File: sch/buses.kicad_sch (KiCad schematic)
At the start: 20 parts, among them U1 74AC00, U2 74HC74, U3 DS1135Z, U4 74LS32, U5 74LS11

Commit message: New address decoder
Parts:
- added unit 1 of U1
- C10, C9: value 100nF -> (none)
- C5, C6, C7, C8: value 10nF -> (none)
- D1: value 1N5817 -> (none)
- R1: value ~ -> (none)
- U1: value 74AC00 -> (none); footprint Package_SO:TSSOP-14_4.4x5mm_P0.65mm -> (none)
- U2: value 74HC74 -> (none)
- U3: value DS1135Z -> (none)
- U3: value DS1135Z -> (none); footprint Package_SO:SO-8_5.3x6.2mm_P1.27mm -> (none)
- U4: value 74LS32 -> (none)
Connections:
- net +5V: no longer U4.4, U4.5
- net CLK: now also U4.4
- net CPU_R/~{W}: now also U4.5, U1.1, U1.2; no longer BDT1.1 (A->B)
- net MEM_WR: now reaches U4.6
- net BUS_IN_EN renamed DATA_BUS_EN
- net CPU_BUS_ENABLE renamed CPU_BUS_EN
- net LATCH_~{Load}: no longer names the net of LATCH1.11 (Load), U5.6
- net LATCH_~{OE}: no longer names the net of LATCH1.1 (OE), U1.8, U4.2
- new net CPU_W/~{R}: BDT1.1 (A->B), U1.3
- no-connect marks 9 -> 8
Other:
- moved on the sheet: D1, R1, U1B, U1C, U1D, U2A, U3A, U4A, U4B, U5A, U5B

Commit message: Board layout, addr bus
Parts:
- removed RP3, RP4, RP5: 1K, Resistor_THT:R_Array_SIP9, symbol Device:R_Network08
- added R12, R13, R14, R15, R16, R17, R18, R19, R20, R21, R22, R23, R32, R33, R34, R35: 1K, Resistor_SMD:R_0603_1608Metric, symbol Device:R
- added R3: 10K, Resistor_SMD:R_1206_3216Metric_Pad1.30x1.75mm_HandSolder, symbol Device:R
- C10, C9: value (none) -> 100nF; footprint (none) -> Capacitor_SMD:C_1206_3216Metric_Pad1.33x1.80mm_HandSolder
- C5, C6, C7, C8: value (none) -> 10nF; footprint (none) -> Capacitor_SMD:C_1206_3216Metric_Pad1.33x1.80mm_HandSolder
- D1: value (none) -> 1N5817; footprint (none) -> Diode_THT:D_A-405_P7.62mm_Horizontal
- R1: value (none) -> 1K; footprint (none) -> Resistor_SMD:R_1206_3216Metric_Pad1.30x1.75mm_HandSolder
- RP1, RP2: value 1K -> (none); footprint Resistor_THT:R_Array_SIP9 -> (none)
- U1: value (none) -> 74AC00; footprint (none) -> Package_SO:TSSOP-14_4.4x5mm_P0.65mm
- U2: value (none) -> 74HC74; footprint (none) -> Package_SO:SOIC-14_3.9x8.7mm_P1.27mm
- U3: value (none) -> DS1135Z; footprint (none) -> Package_SO:SO-8_5.3x6.2mm_P1.27mm
- U4: value (none) -> 74HC32; footprint (none) -> Package_SO:SO-14_5.3x10.2mm_P1.27mm
- U5: value 74LS11 -> 74HC11; footprint (none) -> Package_SO:SO-14_5.3x10.2mm_P1.27mm
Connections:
- net +5V: now also R3.1; no longer U4.10, U4.9, U5.10, U5.11, U5.9
- net A0: now also R35.2
- net A1: now also R34.2
- net A10: now also RP2.3 (R2)
- net A11: now also RP2.2 (R1)
- net A12: now also R23.2
- net A13: now also R22.2
- net A14: now also R21.2
- net A15: now also R20.2
- net A16: now also R19.2
- net A17: now also R18.2
- net A18: now also R17.2
- net A19: now also R16.2
- net A2: now also R33.2
- net A20: now also R15.2
- net A21: now also R14.2
- net A22: now also R13.2
- net A23: now also R12.2
- net A3: now also R32.2
- net A4: now also RP2.9 (R8)
- net A5: now also RP2.8 (R7)
- net A6: now also RP2.7 (R6)
- net A7: now also RP2.6 (R5)
- net A8: now also RP2.5 (R4)
- net A9: now also RP2.4 (R3)
- net CLK: no longer U5.2, U5.4
- net DBA0: no longer RP2.2 (R1)
- net DBA1: no longer RP2.3 (R2)
- net DBA2: no longer RP2.4 (R3)
- net DBA3: no longer RP2.5 (R4)
- net DBA4: no longer RP2.6 (R5)
- net DBA5: no longer RP2.7 (R6)
- net DBA6: no longer RP2.8 (R7)
- net DBA7: no longer RP2.9 (R8)
- net GND: now also R12.1, R13.1, R14.1, R15.1, R16.1, R17.1, R18.1, R19.1, R20.1, R21.1, R22.1, R23.1, R32.1, R33.1, R34.1, R35.1
- net BUS_OPCODE: now reaches U5.8
- net VA: now reaches U4.8
- net CPU_R/~{W} renamed CPU_R~{W}
- net CPU_W/~{R} renamed CPU_W~{R}
- net MEM_WR renamed MEM_W~{R}
- net READY_IN: no longer names the net of U2.2 (D)
- net READY_IN: now also R3.2
- new net CPU_VDA: U4.10, U5.10, U5.11
- new net CPU_VPA: U4.9, U5.9
- new net ~{CLK}: U5.2, U5.4
- no-connect marks 8 -> 6
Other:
- note added: "When there is valid data and program address on the BUS, this indicates the fetching of an OPCODE."
- moved on the sheet: U1A, U3B, U3C, U3D, U4B, U4C, U4D, U5C

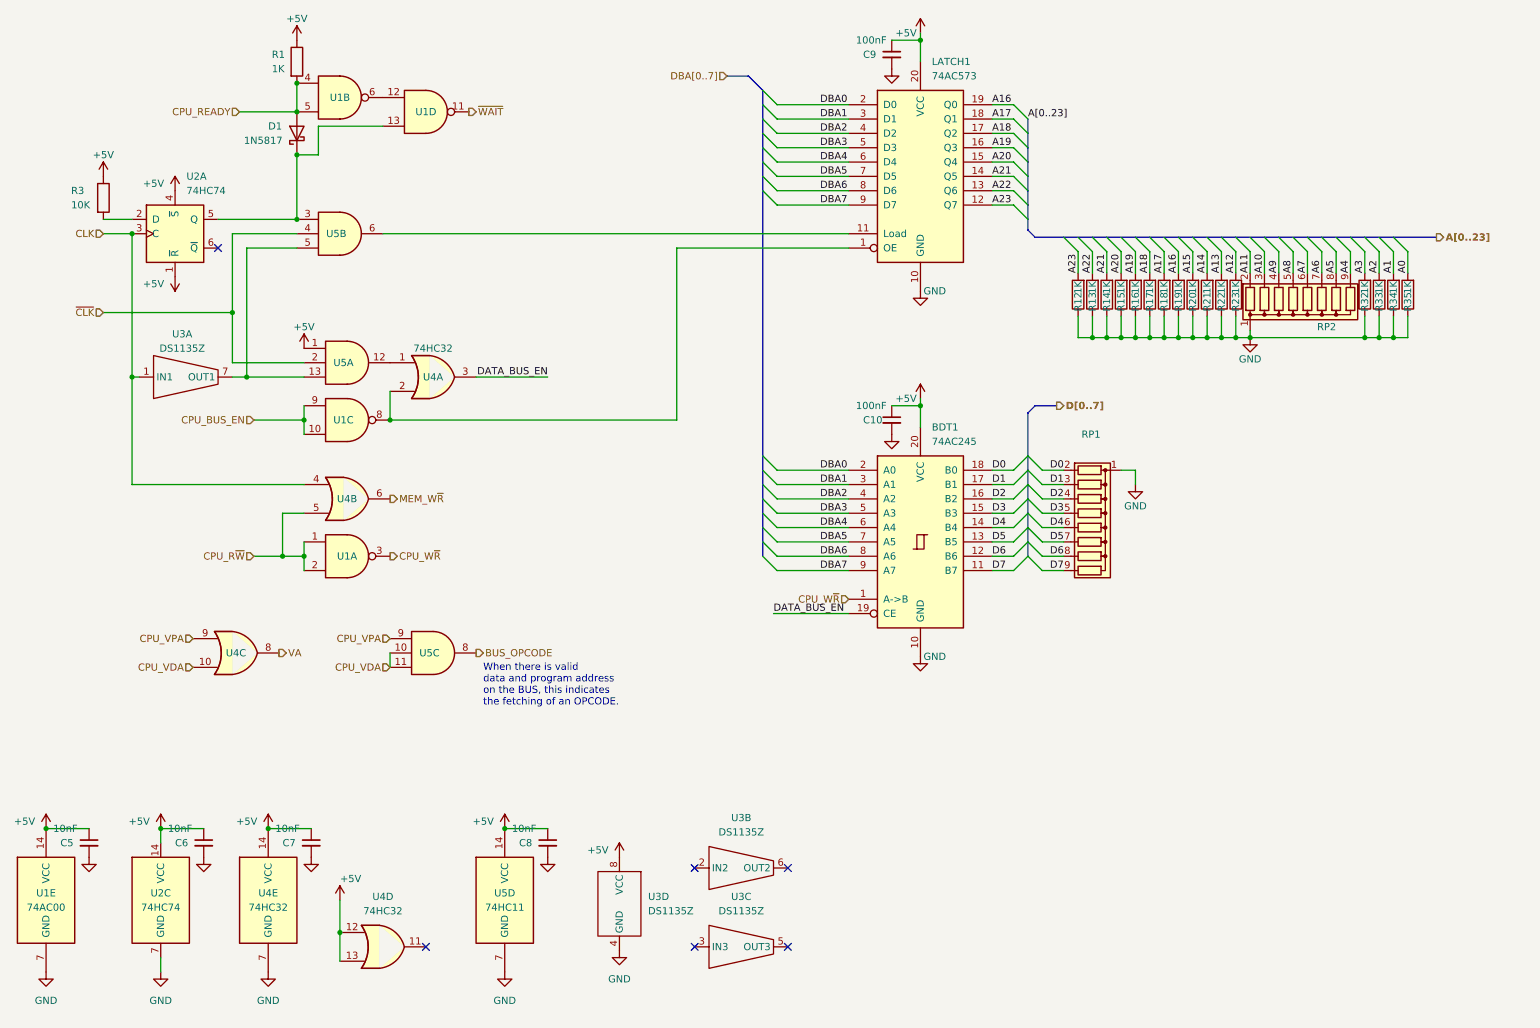
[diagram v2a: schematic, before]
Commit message: More routing, USB iface
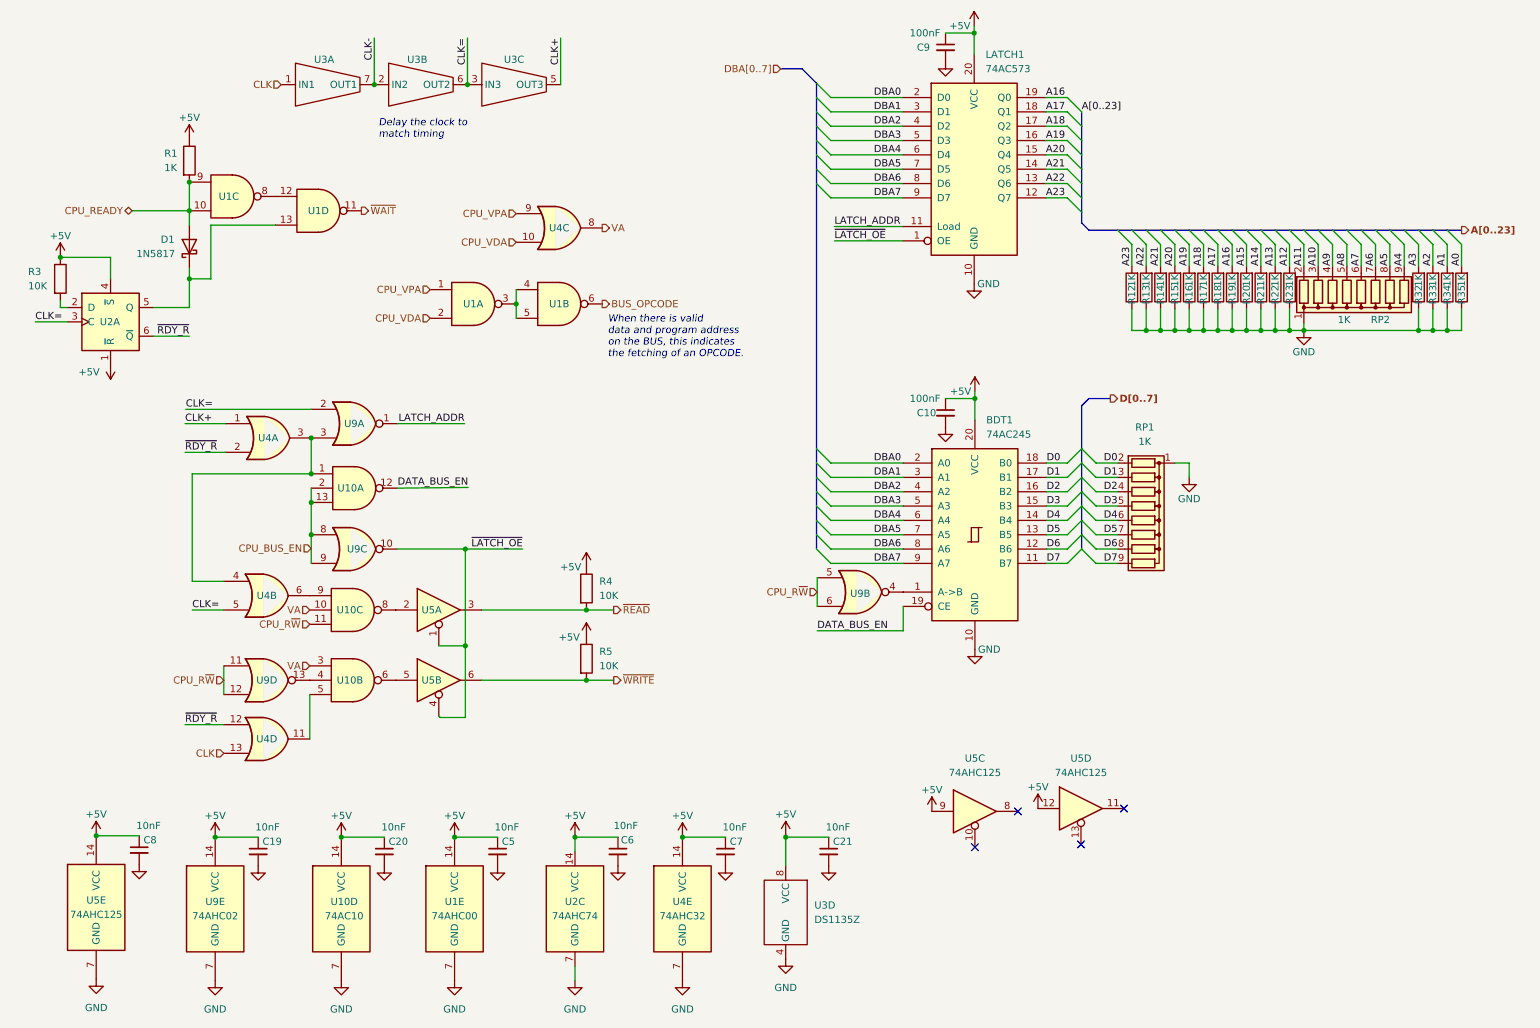
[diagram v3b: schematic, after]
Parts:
- removed U5: 74HC11, Package_SO:SO-14_5.3x10.2mm_P1.27mm, symbol 74xx:74LS11
- added C19, C20, C21: 10nF, Capacitor_SMD:C_0603_1608Metric, symbol Device:C_Small
- added R4, R5: 10K, Resistor_SMD:R_1206_3216Metric_Pad1.30x1.75mm_HandSolder, symbol Device:R
- added U10: 74AC10, Package_SO:TSSOP-14_4.4x5mm_P0.65mm, symbol 74xx:74LS10
- added U5: 74AHC125, Package_SO:TSSOP-14_4.4x5mm_P0.65mm, symbol 74xx:74LS125
- added U9: 74AHC02, Package_SO:TSSOP-14_4.4x5mm_P0.65mm, symbol 74xx:74LS02
- C5, C6, C7, C8: footprint Capacitor_SMD:C_1206_3216Metric_Pad1.33x1.80mm_HandSolder -> Capacitor_SMD:C_0603_1608Metric
- R1: footprint Resistor_SMD:R_1206_3216Metric_Pad1.30x1.75mm_HandSolder -> Resistor_SMD:R_0603_1608Metric
- RP1, RP2: value (none) -> 1K; footprint (none) -> Resistor_THT:R_Array_SIP9
- U1: value 74AC00 -> 74AHC00
- U2: value 74HC74 -> 74AHC74; footprint Package_SO:SOIC-14_3.9x8.7mm_P1.27mm -> Package_SO:TSSOP-14_4.4x5mm_P0.65mm
- U4: value 74HC32 -> 74AHC32; footprint Package_SO:SO-14_5.3x10.2mm_P1.27mm -> Package_SO:TSSOP-14_4.4x5mm_P0.65mm
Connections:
- net +5V: now also C19.1, C20.1, C21.1, R4.1, R5.1, U10.14 (VCC), U5.12, U5.14 (VCC), U5.9, U9.14 (VCC); no longer U4.12, U4.13
- net BUS_OPCODE: now also U1.6
- net CLK: now also U4.13; no longer U2.3 (C), U4.4
- net CPU_BUS_EN: now also U10.13, U10.2, U9.8, U9.9; no longer U1.10, U1.9
- net CPU_READY: now also U1.10, U1.9; no longer U1.4, U1.5
- net CPU_R~{W}: now also U10.11, U9.11, U9.12, U9.5, U9.6; no longer U1.1, U1.2, U4.5
- net CPU_VDA: now also U1.2
- net CPU_VPA: now also U1.1
- net DATA_BUS_EN: now also U10.12; no longer U4.3
- net GND: now also C19.2, C20.2, C21.2, U10.7 (GND), U5.7 (GND), U9.7 (GND)
- net VA: now also U10.10, U10.3
- net at U1.12: now also U1.8; no longer U1.6
- net CLK+: now reaches U4.1
- net CLK+: now also U3.5 (OUT3)
- net CLK-: now reaches U3.7 (OUT1)
- net CLK-: now also U3.2 (IN2)
- net LATCH_ADDR: now reaches LATCH1.11 (Load)
- net LATCH_ADDR: now also U9.1
- net CLK=: now reaches U3.3 (IN3)
- net CLK=: now also U2.3 (C), U3.6 (OUT2), U4.5, U9.2
- net at U4.11: now also U10.5
- net ~{RDY_R}: now reaches U2.6 (~{Q})
- net ~{RDY_R}: now also U4.12, U4.2
- net CPU_W~{R}: no longer names the net of U1.3
- net CPU_W~{R}: now also U1.4, U1.5; no longer BDT1.1 (A->B)
- net MEM_W~{R}: no longer names the net of U4.6
- net MEM_W~{R}: now also U10.9
- new net: U10.8, U5.2
- new net: U10.4, U9.13
- new net: U10.6, U5.5
- new net: U10.1, U4.3, U4.4, U9.3
- new net: BDT1.1 (A->B), U9.4
- new net ~{LATCH_OE}: LATCH1.1 (OE), U5.1, U5.4, U9.10
- new net ~{READ}: R4.2, U5.3
- new net ~{WRITE}: R5.2, U5.6
- no-connect marks 6 -> 4
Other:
- note added: "Delay the clock to match timing"
- moved on the sheet: BDT1, C10, C5, C6, C7, C9, D1, LATCH1, R1, R12, R13, R14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

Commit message: Pivot to 6502
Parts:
- removed C19, C20, C5, C6, C7, C8: 10nF, Capacitor_SMD:C_0603_1608Metric, symbol Device:C_Small
- removed U1: 74AHC00, Package_SO:TSSOP-14_4.4x5mm_P0.65mm, symbol 74xx:74HC00
- removed U10: 74AC10, Package_SO:TSSOP-14_4.4x5mm_P0.65mm, symbol 74xx:74LS10
- removed unit 3 of U2
- removed U4: 74AHC32, Package_SO:TSSOP-14_4.4x5mm_P0.65mm, symbol 74xx:74LS32
- removed U5: 74AHC125, Package_SO:TSSOP-14_4.4x5mm_P0.65mm, symbol 74xx:74LS125
- removed U9: 74AHC02, Package_SO:TSSOP-14_4.4x5mm_P0.65mm, symbol 74xx:74LS02
- added C24, C25, C26, C28: 100nF, Capacitor_SMD:C_0603_1608Metric, symbol Device:C_Small
- added C27, C29, C30, C31: 10nF, Capacitor_SMD:C_0603_1608Metric, symbol Device:C_Small
- added J4: FPGA_Prog, Connector_PinHeader_1.00mm:PinHeader_1x05_P1.00mm_Vertical, symbol Connector_Generic:Conn_01x05
- added R8: 4.7K, Resistor_SMD:R_0603_1608Metric, symbol Device:R
- added R9: 1K, Resistor_SMD:R_0402_1005Metric, symbol Device:R
- added U15: LCMXO2-256ZE-3SG32I, Package_DFN_QFN:QFN-32-1EP_5x5mm_P0.5mm_EP3.1x3.1mm, symbol Custom:﻿MachXO2-256-QFN32
- C21: value 10nF -> 100nF
- U3: value DS1135Z -> DS1135Z-6+
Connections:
- net A10: now also RP2.5 (R4); no longer RP2.3 (R2)
- net A11: now also RP2.4 (R3); no longer RP2.2 (R1)
- net A8: now also RP2.2 (R1); no longer RP2.5 (R4)
- net A9: now also RP2.3 (R2); no longer RP2.4 (R3)
- net BUS_OPCODE: now also U15.20 (PR5B)
- net CLK: now also U15.12 (PB4B)
- net CLK+: now also U15.4 (PL5C)
- net CLK=: now also U15.5 (PL5D)
- net CPU_BUS_EN: now also U15.13 (PB4C)
- net CPU_R~{W}: now also U15.14 (PB4D)
- net CPU_VDA: now also U15.16 (PB9A/SN)
- net CPU_VPA: now also U15.17 (PB9B/SI)
- net DATA_BUS_EN: now also U15.8 (PB2A/CS)
- net GND: now also C24.1, C25.1, C26.1, C27.1, C28.1, C29.1, C30.1, C31.1, J4.4 (Pin_4), R8.2, U15.22 (GND), U15.3 (GND), U15.33 (GND)
- net LATCH_ADDR: now also U15.10 (PB2D/SPISO)
- net VA: now also U15.21 (PR5A)
- net ~{LATCH_OE}: now also U15.9 (PB2C/SCLK)
- net ~{RDY_R}: now also U15.25 (PT9B/PROGRAMN)
- net ~{READ}: now also U15.28 (PT8C/SCL)
- net ~{WAIT}: now also U15.23 (PT9D/DONE)
- net ~{WRITE}: now also U15.27 (PT8D/SDA)
- net RDY_R: now reaches D1.1 (K), U2.5 (Q)
- net CPU_W~{R}: now reaches BDT1.1 (A->B)
- net CPU_W~{R}: now also U15.11 (PB4A)
- new net: R9.1, U15.26 (PT9A/JTAGENB)
- new net +3V3: C24.2, C25.2, C26.2, C27.2, C28.2, C29.2, C30.2, C31.2, R9.2, U15.15 (VCCIO2), U15.18 (VCC), U15.19 (VCCIO1), U15.2 (VCC), U15.24 (VCCIO0), U15.31 (VCCIO0), U15.6 (VCCIO3), U15.7 (VCCIO2)
- new net XO2_TCK: J4.2 (Pin_2), R8.1, U15.30 (PT7A/TCK)
- new net XO2_TDI: J4.3 (Pin_3), U15.32 (PT6D/TDI)
- new net XO2_TDO: J4.5 (Pin_5), U15.1 (PT6C/TDO)
- new net XO2_TMS: J4.1 (Pin_1), U15.29 (PT7B/TMS)
- no-connect marks 4 -> 0
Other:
- note added: "IN"
- note added: "OUT"
- moved on the sheet: D1, R1, R3, U2A, U3A, U3B, U3C
